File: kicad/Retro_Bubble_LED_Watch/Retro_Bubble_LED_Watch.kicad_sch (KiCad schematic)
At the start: 21 parts, among them J2 AVR ISP Connector, SW1 MODE, SW2 UP, U2 ATmega328PB-A, U3 DS1337S+

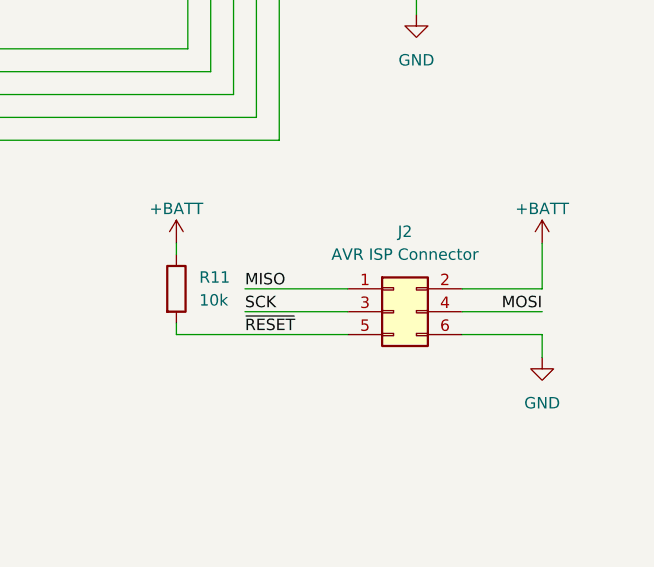
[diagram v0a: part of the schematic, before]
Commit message: added socket and display models
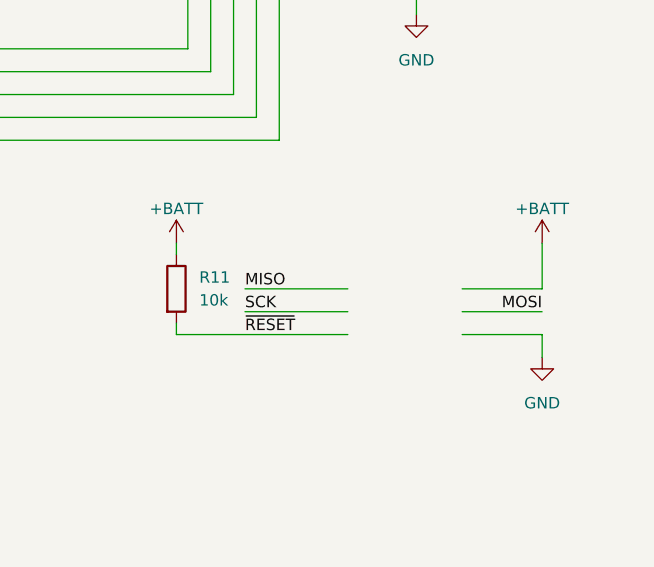
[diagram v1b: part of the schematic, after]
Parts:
- removed J2: AVR ISP Connector, Connector_PinHeader_2.54mm:PinHeader_2x03_P2.54mm_Vertical_SMD, symbol Connector_Generic:Conn_02x03_Odd_Even
- BZ1: footprint (none) -> footprints:FUET-5020
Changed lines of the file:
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@@
-    )
-  )
-  (symbol (lib_id "Connector_Generic:Conn_02x03_Odd_Even") (at 254 85.09 0) (unit 1)
-    (in_bom yes) (on_board yes) (dnp no) (fields_autoplaced)
-    (property "Reference" "J2" (at 255.27 76.2 0)
-      (effects (font (size 1.27 1.27)))
-    )
-    (property "Value" "AVR ISP Connector" (at 255.27 78.74 0)
-      (effects (font (size 1.27 1.27)))
-    )
-    (property "Footprint" "Connector_PinHeader_2.54mm:PinHeader_2x03_P2.54mm_Vertical_SMD" (at 254 85.09 0)
-      (effects (font (size 1.27 1.27)) hide)
-    )
-    (property "Datasheet" "~" (at 254 85.09 0)
-      (effects (font (size 1.27 1.27)) hide)
-    )
-    (pin "2")
-    (pin "3")
-    (pin "4")
-    (pin "1")
-    (pin "5")
-    (pin "6")
-    (instances
-      (project "Retro_Bubble_LED_Watch"
-        (path "/241adb6f-f268-45e9-b7ae-ba5c9ee53a74"
-          (reference "J2") (unit 1)
-        )
-      )
     )
   )
@@
       (effects (font (size 1.27 1.27)) (justify left))
     )
-    (property "Footprint" "" (at 28.575 81.28 90)
-      (effects (font (size 1.27 1.27)) hide)
-    )
+    (property "Footprint" "footprints:FUET-5020" (at 28.575 81.28 90)
+      (effects (font (size 1.27 1.27)) hide)
+    )

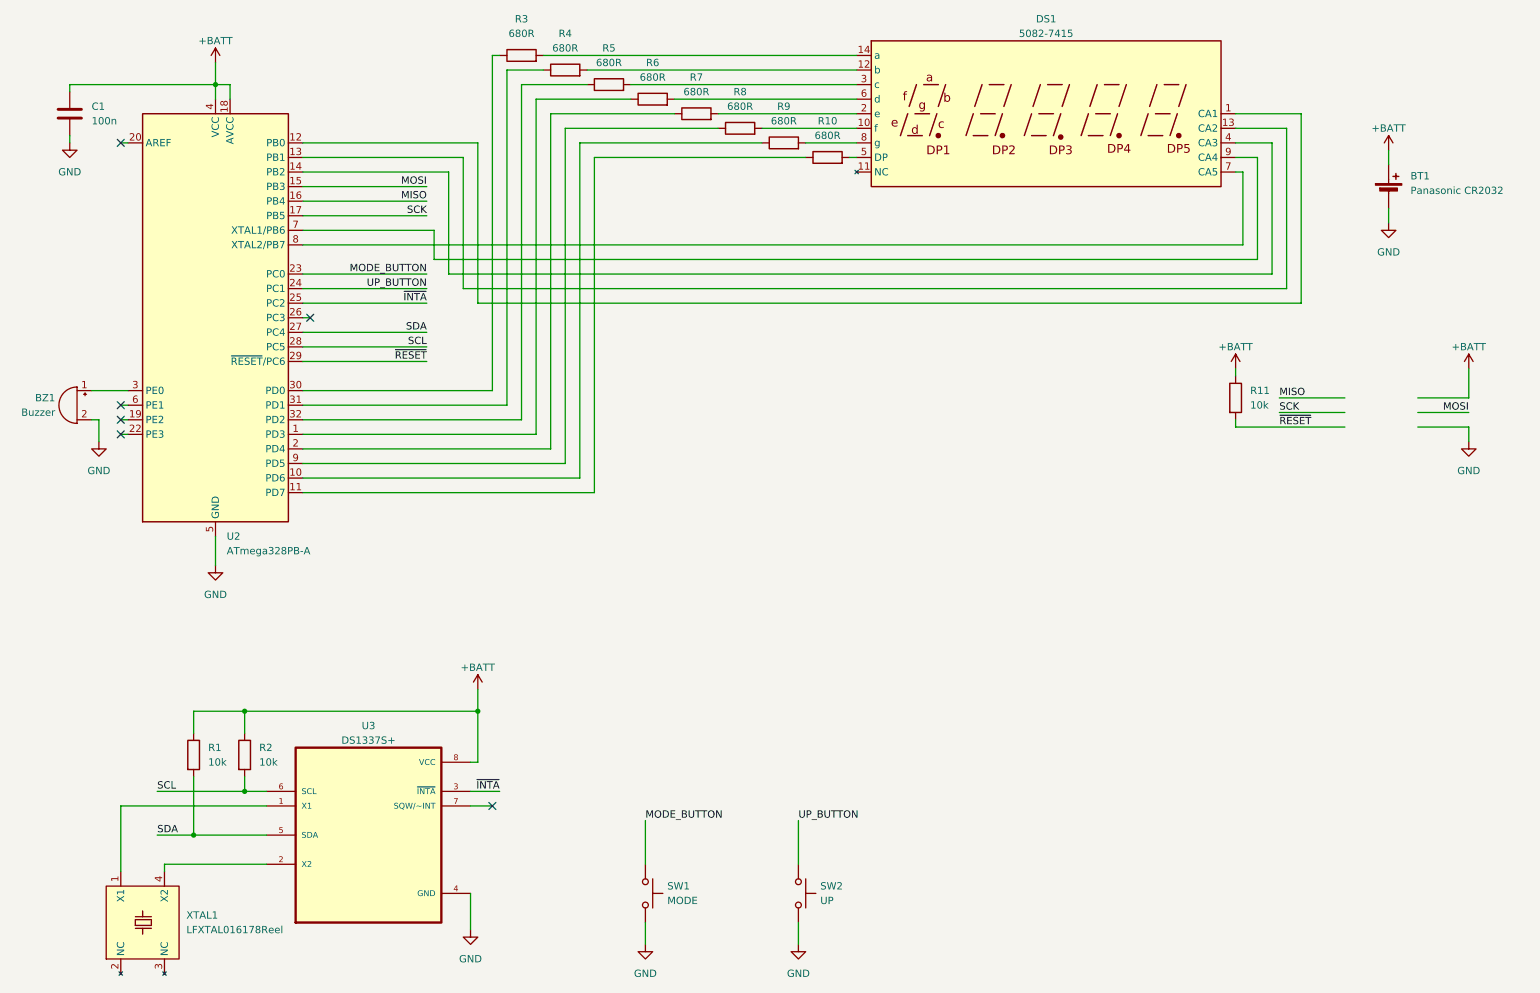
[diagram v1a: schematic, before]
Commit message: final PCB design + gerber + initial models
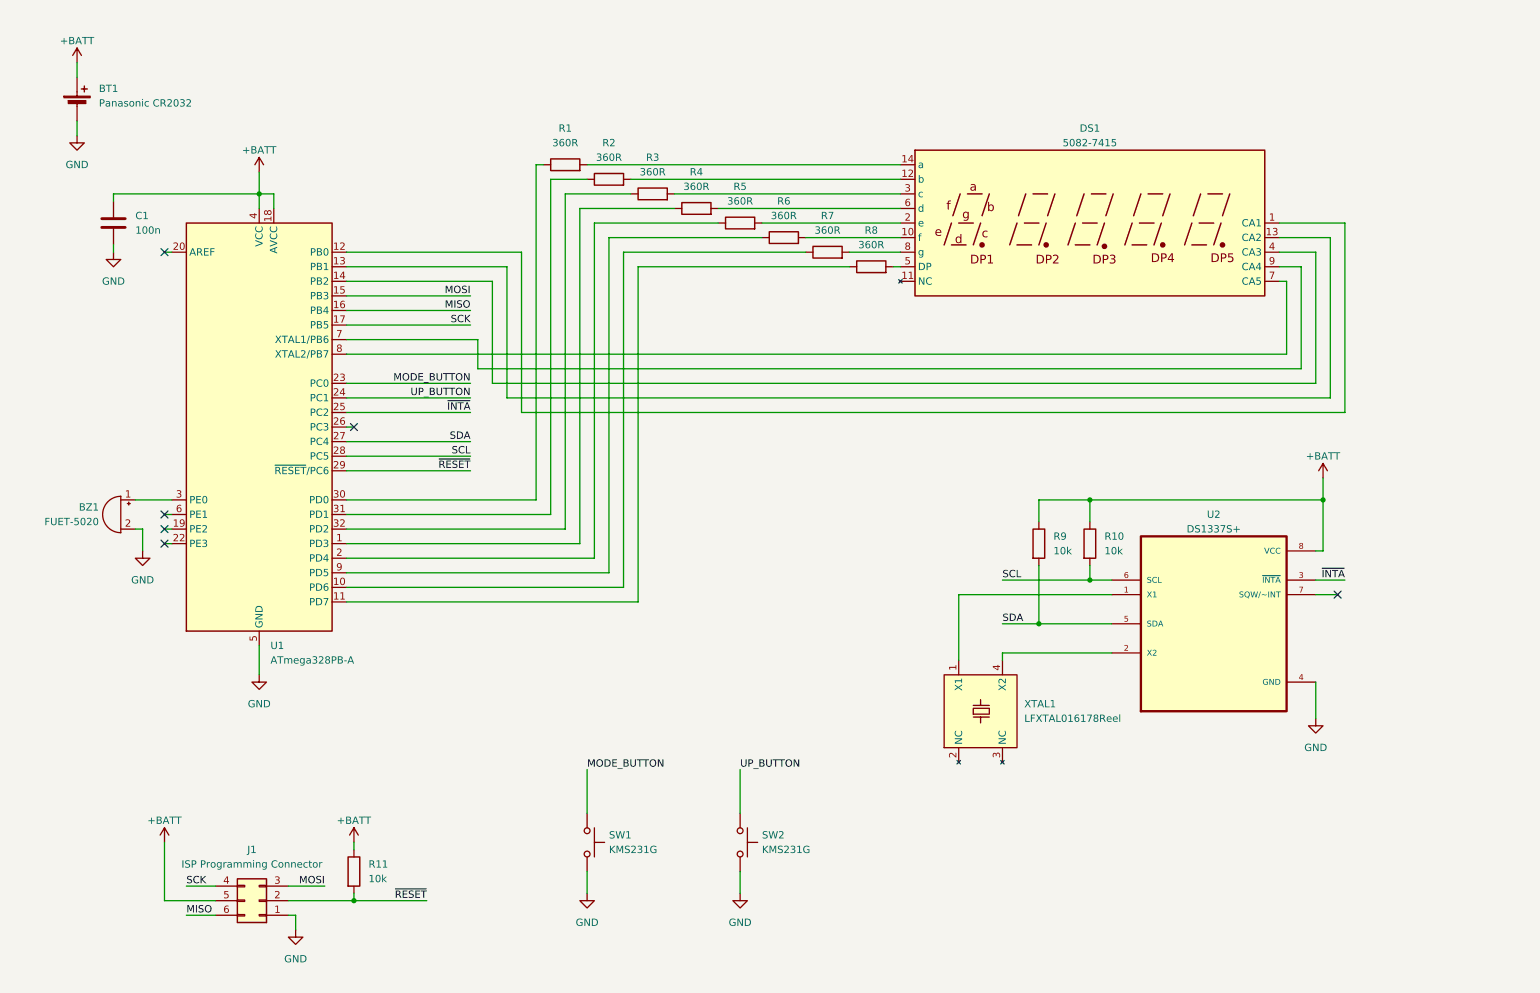
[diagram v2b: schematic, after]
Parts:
- added J1: ISP Programming Connector, Connector_PinHeader_1.27mm:PinHeader_2x03_P1.27mm_Vertical, symbol Connector_Generic:Conn_02x03_Counter_Clockwise
- BZ1: value Buzzer -> FUET-5020
- R1: renamed from R3; value 680R -> 360R
- R2: renamed from R4; value 680R -> 360R
- R3: renamed from R5; value 680R -> 360R
- R4: renamed from R6; value 680R -> 360R
- R5: renamed from R7; value 680R -> 360R
- R6: renamed from R8; value 680R -> 360R
- R7: renamed from R9; value 680R -> 360R
- R8: renamed from R10; value 680R -> 360R
- SW1: value MODE -> KMS231G
- SW2: value UP -> KMS231G
- renumbered R2 to R10, R1 to R9, U2 to U1, U3 to U2
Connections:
- net +BATT: now also J1.5 (Pin_5)
- net GND: now also J1.1 (Pin_1)
- net MISO: now also J1.6 (Pin_6)
- net MOSI: now also J1.3 (Pin_3)
- net SCK: now also J1.4 (Pin_4)
- net ~{RESET}: now also J1.2 (Pin_2)
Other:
- moved on the sheet: BT1, BZ1, C1, DS1, R1, R10, R2, R3, R4, R5, R6, R7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

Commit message: finished models
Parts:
- R1, R2, R3, R4, R5, R6, R7, R8: value 360R -> 330R
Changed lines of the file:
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@@
       (effects (font (size 1.27 1.27)))
     )
-    (property "Value" "360R" (at 151.13 50.8 90)
+    (property "Value" "330R" (at 151.13 50.8 90)
       (effects (font (size 1.27 1.27)))
     )
@@
       (effects (font (size 1.27 1.27)))
     )
-    (property "Value" "360R" (at 135.89 45.72 90)
+    (property "Value" "330R" (at 135.89 45.72 90)
       (effects (font (size 1.27 1.27)))
     )
@@
       (effects (font (size 1.27 1.27)))
     )
-    (property "Value" "360R" (at 128.27 43.18 90)
+    (property "Value" "330R" (at 128.27 43.18 90)
       (effects (font (size 1.27 1.27)))
     )
@@
       (effects (font (size 1.27 1.27)))
     )
-    (property "Value" "360R" (at 143.51 48.26 90)
+    (property "Value" "330R" (at 143.51 48.26 90)
       (effects (font (size 1.27 1.27)))
     )
@@
       (effects (font (size 1.27 1.27)))
     )
-    (property "Value" "360R" (at 113.03 38.1 90)
+    (property "Value" "330R" (at 113.03 38.1 90)
       (effects (font (size 1.27 1.27)))
     )
@@
       (effects (font (size 1.27 1.27)))
     )
-    (property "Value" "360R" (at 166.37 55.88 90)
+    (property "Value" "330R" (at 166.37 55.88 90)
       (effects (font (size 1.27 1.27)))
     )
@@
       (effects (font (size 1.27 1.27)))
     )
-    (property "Value" "360R" (at 158.75 53.34 90)
+    (property "Value" "330R" (at 158.75 53.34 90)
       (effects (font (size 1.27 1.27)))
     )
@@
       (effects (font (size 1.27 1.27)))
     )
-    (property "Value" "360R" (at 120.65 40.64 90)
-      (effects (font (size 1.27 1.27)))
-    )
+    (property "Value" "330R" (at 120.65 40.64 90)
+      (effects (font (size 1.27 1.27)))
+    )

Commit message: finished rev. 1.0
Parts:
- BT1: value Panasonic CR2032 -> Panasonic CR2032/BN
- DS1: value 5082-7415 -> HP 5082-7415
- R1, R2, R3, R4, R5, R6, R7, R8: value 330R -> 680R
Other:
- note added: "Mounted in CONNFLY DS1001-02-14N13 SMD DIP14 Socket"
- note added: "Mounted in KEYSTONE 1060 Battery Holder"
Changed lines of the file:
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@@
     (rev "1.0")
     (company "Szymon Bartosik")
+    (comment 1 "the disisplay if 5V logic level is used!")
+    (comment 2 "Important notice: Before programming, always remove the battery and possibly ")
     (comment 3 "All capacitors are ±10% MLCC X7R 0603 type unless otherwise specified.")
     (comment 4 "All resistors are ±5% 0603 type unless otherwise specified.")
@@
     (stroke (width 0) (type default))
   )
-  (wire (pts (xy 27.94 34.29) (xy 27.94 36.83))
+  (wire (pts (xy 27.94 34.29) (xy 27.94 38.1))
     (stroke (width 0) (type default))
   )
@@
     (stroke (width 0) (type default))
   )
-  (wire (pts (xy 27.94 24.13) (xy 27.94 26.67))
+  (wire (pts (xy 27.94 22.86) (xy 27.94 26.67))
     (stroke (width 0) (type default))
   )
@@
   (wire (pts (xy 38.1 100.33) (xy 44.45 100.33))
     (stroke (width 0) (type default))
+  )
+  (rectangle (start 170.18 33.02) (end 240.03 67.31)
+    (stroke (width 0) (type dash))
+    (fill (type none))
+  )
+  (rectangle (start 24.13 26.67) (end 31.75 34.29)
+    (stroke (width 0) (type dash))
+    (fill (type none))
+  )
+  (text "Mounted in CONNFLY DS1001-02-14N13 SMD DIP14 Socket"
+    (at 175.26 31.75 0)
+    (effects (font (size 1.27 1.27)) (justify left bottom))
+  )
+  (text "Mounted in KEYSTONE 1060 Battery Holder" (at 30.48 25.4 0)
+    (effects (font (size 1.27 1.27)) (justify left bottom))
   )
   (label "SDA" (at 96.52 90.17 180) (fields_autoplaced)
@@
     (effects (font (size 1.27 1.27)) (justify left bottom))
   )
-  (symbol (lib_id "power:GND") (at 27.94 36.83 0) (unit 1)
-    (in_bom yes) (on_board yes) (dnp no) (fields_autoplaced)
-    (property "Reference" "#PWR02" (at 27.94 43.18 0)
-      (effects (font (size 1.27 1.27)) hide)
-    )
-    (property "Value" "GND" (at 27.94 41.91 0)
-      (effects (font (size 1.27 1.27)))
-    )
-    (property "Footprint" "" (at 27.94 36.83 0)
-      (effects (font (size 1.27 1.27)) hide)
-    )
-    (property "Datasheet" "" (at 27.94 36.83 0)
+  (symbol (lib_id "power:GND") (at 27.94 38.1 0) (unit 1)
+    (in_bom yes) (on_board yes) (dnp no) (fields_autoplaced)
+    (property "Reference" "#PWR02" (at 27.94 44.45 0)
+      (effects (font (size 1.27 1.27)) hide)
+    )
+    (property "Value" "GND" (at 27.94 43.18 0)
+      (effects (font (size 1.27 1.27)))
+    )
+    (property "Footprint" "" (at 27.94 38.1 0)
+      (effects (font (size 1.27 1.27)) hide)
+    )
+    (property "Datasheet" "" (at 27.94 38.1 0)
       (effects (font (size 1.27 1.27)) hide)
     )
@@
       (effects (font (size 1.27 1.27)))
     )
-    (property "Value" "330R" (at 151.13 50.8 90)
+    (property "Value" "680R" (at 151.13 50.8 90)
       (effects (font (size 1.27 1.27)))
     )
@@
       (effects (font (size 1.27 1.27)))
     )
-    (property "Value" "330R" (at 135.89 45.72 90)
+    (property "Value" "680R" (at 135.89 45.72 90)
       (effects (font (size 1.27 1.27)))
     )
@@
       (effects (font (size 1.27 1.27)))
     )
-    (property "Value" "330R" (at 128.27 43.18 90)
+    (property "Value" "680R" (at 128.27 43.18 90)
       (effects (font (size 1.27 1.27)))
     )
@@
       (effects (font (size 1.27 1.27)) (justify left))
     )
-    (property "Value" "Panasonic CR2032" (at 31.75 31.1785 0)
+    (property "Value" "Panasonic CR2032/BN" (at 31.75 31.1785 0)
       (effects (font (size 1.27 1.27)) (justify left))
     )
@@
       (effects (font (size 1.27 1.27)))
     )
-    (property "Value" "5082-7415" (at 204.47 38.1 0)
+    (property "Value" "HP 5082-7415" (at 204.47 38.1 0)
       (effects (font (size 1.27 1.27)))
     )
@@
       (effects (font (size 1.27 1.27)))
     )
-    (property "Value" "330R" (at 143.51 48.26 90)
+    (property "Value" "680R" (at 143.51 48.26 90)
       (effects (font (size 1.27 1.27)))
     )
@@
       (effects (font (size 1.27 1.27)))
     )
-    (property "Value" "330R" (at 113.03 38.1 90)
+    (property "Value" "680R" (at 113.03 38.1 90)
       (effects (font (size 1.27 1.27)))
     )
@@
       (effects (font (size 1.27 1.27)))
     )
-    (property "Value" "330R" (at 166.37 55.88 90)
+    (property "Value" "680R" (at 166.37 55.88 90)
       (effects (font (size 1.27 1.27)))
     )
@@
       (effects (font (size 1.27 1.27)))
     )
-    (property "Value" "330R" (at 158.75 53.34 90)
+    (property "Value" "680R" (at 158.75 53.34 90)
       (effects (font (size 1.27 1.27)))
     )
@@
       (effects (font (size 1.27 1.27)))
     )
-    (property "Value" "330R" (at 120.65 40.64 90)
+    (property "Value" "680R" (at 120.65 40.64 90)
       (effects (font (size 1.27 1.27)))
     )
@@
     )
   )
-  (symbol (lib_id "power:+BATT") (at 27.94 24.13 0) (unit 1)
-    (in_bom yes) (on_board yes) (dnp no) (fields_autoplaced)
-    (property "Reference" "#PWR01" (at 27.94 27.94 0)
-      (effects (font (size 1.27 1.27)) hide)
-    )
-    (property "Value" "+BATT" (at 27.94 20.32 0)
-      (effects (font (size 1.27 1.27)))
-    )
-    (property "Footprint" "" (at 27.94 24.13 0)
-      (effects (font (size 1.27 1.27)) hide)
-    )
-    (property "Datasheet" "" (at 27.94 24.13 0)
-      (effects (font (size 1.27 1.27)) hide)
-    )
+  (symbol (lib_id "power:+BATT") (at 27.94 22.86 0) (unit 1)
+    (in_bom yes) (on_board yes) (dnp no) (fields_autoplaced)
+    (property "Reference" "#PWR01" (at 27.94 26.67 0)
+      (effects (font (size 1.27 1.27)) hide)
+    )
+    (property "Value" "+BATT" (at 27.94 19.05 0)
+      (effects (font (size 1.27 1.27)))
+    )
+    (property "Footprint" "" (at 27.94 22.86 0)
+      (effects (font (size 1.27 1.27)) hide)
+    )
+    (property "Datasheet" "" (at 27.94 22.86 0)
+      (effects (font (size 1.27 1.27)) hide)
+    )

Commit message: Rev. 1.1
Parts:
- removed BZ1: FUET-5020, footprints:FUET-5020, symbol Device:Buzzer
- added C2, C3: 100n, Capacitor_SMD:C_0603_1608Metric, symbol Device:C
- added J2: Pad Connector, footprints:Pad_Conn_2x1_2x1mm_2.54mm, symbol Connector_Generic:Conn_01x02
- BT1: value Panasonic CR2032/BN -> 3V; footprint Battery:BatteryHolder_Keystone_1058_1x2032 -> Battery:BatteryHolder_Keystone_1060_1x2032; Manufacturer (none) -> PANASONIC; Model (none) -> CR2032/BN; Socket  (none) -> KEYSTONE 1060
- C1: Manufacturer (none) -> SAMSUNG; Model (none) -> CL10B104KA8NFNC
- DS1: value HP 5082-7415 -> 5082-7415; Manufacturer (none) -> HP; Socket (none) -> CONNFLY DS1001-02-14N13
- J1: value ISP Programming Connector -> 20021111-00006T4LF; Manufacturer (none) -> AMPHENOL COMMUNICATIONS SOLUTIONS
- R1, R2, R3, R4, R5, R6, R7, R8: value 680R -> 330R; Manufacturer (none) -> PANASONIC; Model (none) -> ERJ3EKF3300V
- R10, R11, R9: Manufacturer (none) -> PANASONIC; Model (none) -> ERJ3EKF1002V
- SW1, SW2: Manufacturer (none) -> C&K; Model (none) -> KMS231GLFS
- U1: Manufacturer (none) -> MICROCHIP
- U2: Manufacturer (none) -> MAXIM INTEGRATED
- XTAL1: footprint Crystal:Crystal_SMD_SeikoEpson_MC306-4Pin_8.0x3.2mm_HandSoldering -> footprints:LFXTAL016178Reel; Manufacturer (none) -> IQD FREQUENCY PRODUCTS
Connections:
- net +BATT: now also C2.1
- net GND: now also C2.2, C3.2, J2.1 (Pin_1)
- net at U1.20 (AREF): now also C3.1
- net at U1.3 (PE0): now also J2.2 (Pin_2)
- no-connect marks 6 -> 5
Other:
- note added: "External Piezo Buzzer d = 20 mm, 4kHz"
- note added: "ISP Programming Connector"
- moved on the sheet: BT1, C1, DS1, R1, R2, R3, R4, R5, R6, R7, R8, SW1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

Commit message: improved schematic readability + fixed component paths
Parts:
- BT1: Model CR2032/BN -> (none); Part Number (none) -> CR2032/BN
- C1, C2, C3: Model CL10B104KA8NFNC -> (none); Package (none) -> 0603; Part Number (none) -> CL10B104KA8NFNC
- DS1: Package (none) -> DIP-14; Part Number (none) -> 5082-7415
- J1: value 20021111-00006T4LF -> 2x3 Goldpin Header; Part Number (none) -> 20021111-00006T4LF
- J2: now left out of the parts list
- R1, R2, R3, R4, R5, R6, R7, R8: Model ERJ3EKF3300V -> (none); Package (none) -> 0603; Part Number (none) -> ERJ3EKF3300V
- R10, R11, R9: Model ERJ3EKF1002V -> (none); Package (none) -> 0603; Part Number (none) -> ERJ3EKF1002V
- SW1, SW2: value KMS231G -> Microswitch; Model KMS231GLFS -> (none); Part Number (none) -> KMS231GLFS
- U1: Package (none) -> TQFP-32
- U2: Package (none) -> SOIC-8
- XTAL1: value LFXTAL016178Reel -> 32.678 kHz; Part Number (none) -> LFXTAL016178
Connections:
- net segment.f: now reaches R6.1, U1.9 (PD5)
- net segment.d: now reaches R4.1, U1.1 (PD3)
- net segment.g: now reaches R7.1, U1.10 (PD6)
- net segment.dp: now reaches R8.1, U1.11 (PD7)
- net cathode.CA1: now reaches DS1.1 (CA1), U1.12 (PB0)
- net cathode.CA2: now reaches DS1.13 (CA2), U1.13 (PB1)
- net cathode.CA3: now reaches DS1.4 (CA3), U1.14 (PB2)
- net segment.e: now reaches R5.1, U1.2 (PD4)
- net segment.a: now reaches R1.1, U1.30 (PD0)
- net segment.b: now reaches R2.1, U1.31 (PD1)
- net segment.c: now reaches R3.1, U1.32 (PD2)
- net cathode.CA4: now reaches DS1.9 (CA4), U1.7 (XTAL1/PB6)
- net cathode.CA5: now reaches DS1.7 (CA5), U1.8 (XTAL2/PB7)
- net MISO renamed ISP.MISO
- net MODE_BUTTON: no longer names the net of SW1.1, U1.23 (PC0)
- net MOSI renamed ISP.MOSI
- net SCK renamed ISP.SCK
- net SCL renamed RTC.SCL
- net SDA renamed RTC.SDA
- net UP_BUTTON: no longer names the net of SW2.1, U1.24 (PC1)
- net ~{INTA} renamed RTC.~{INTA}
- net ~{RESET} renamed ISP.~{RESET}
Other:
- note added: "External Piezo Buzzer Connector"
- note added: "MODE Button"
- note added: "UP Button"
- note removed: "External Piezo Buzzer d = 20 mm, 4kHz"
- moved on the sheet: BT1, C1, C2, C3, DS1, J1, J2, R1, R10, R11, R2, R3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
